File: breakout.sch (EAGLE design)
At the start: 21 parts

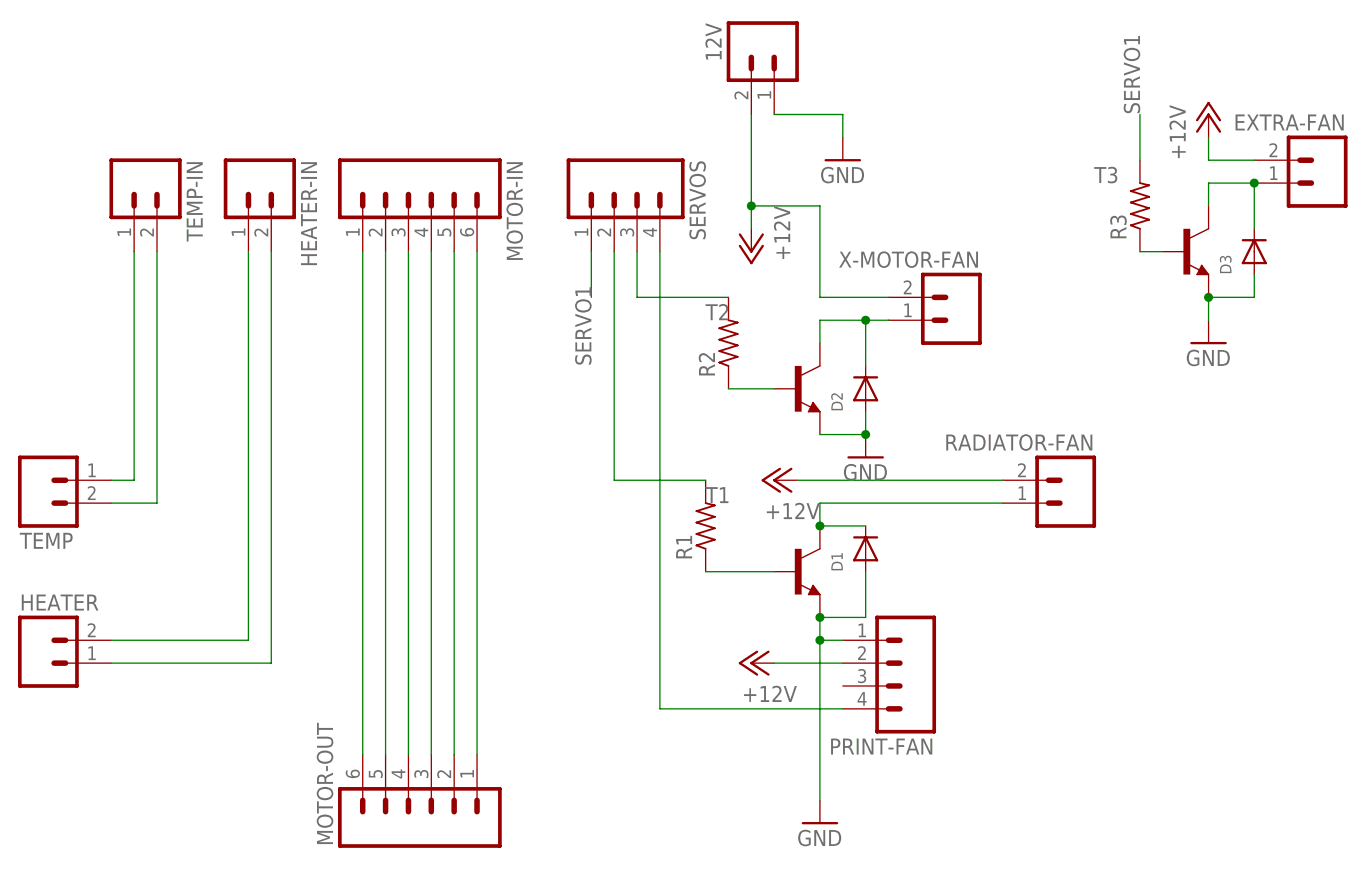
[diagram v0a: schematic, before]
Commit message: Adjusted to 2mm spacing for motor connector, and moved some connectors a bit.
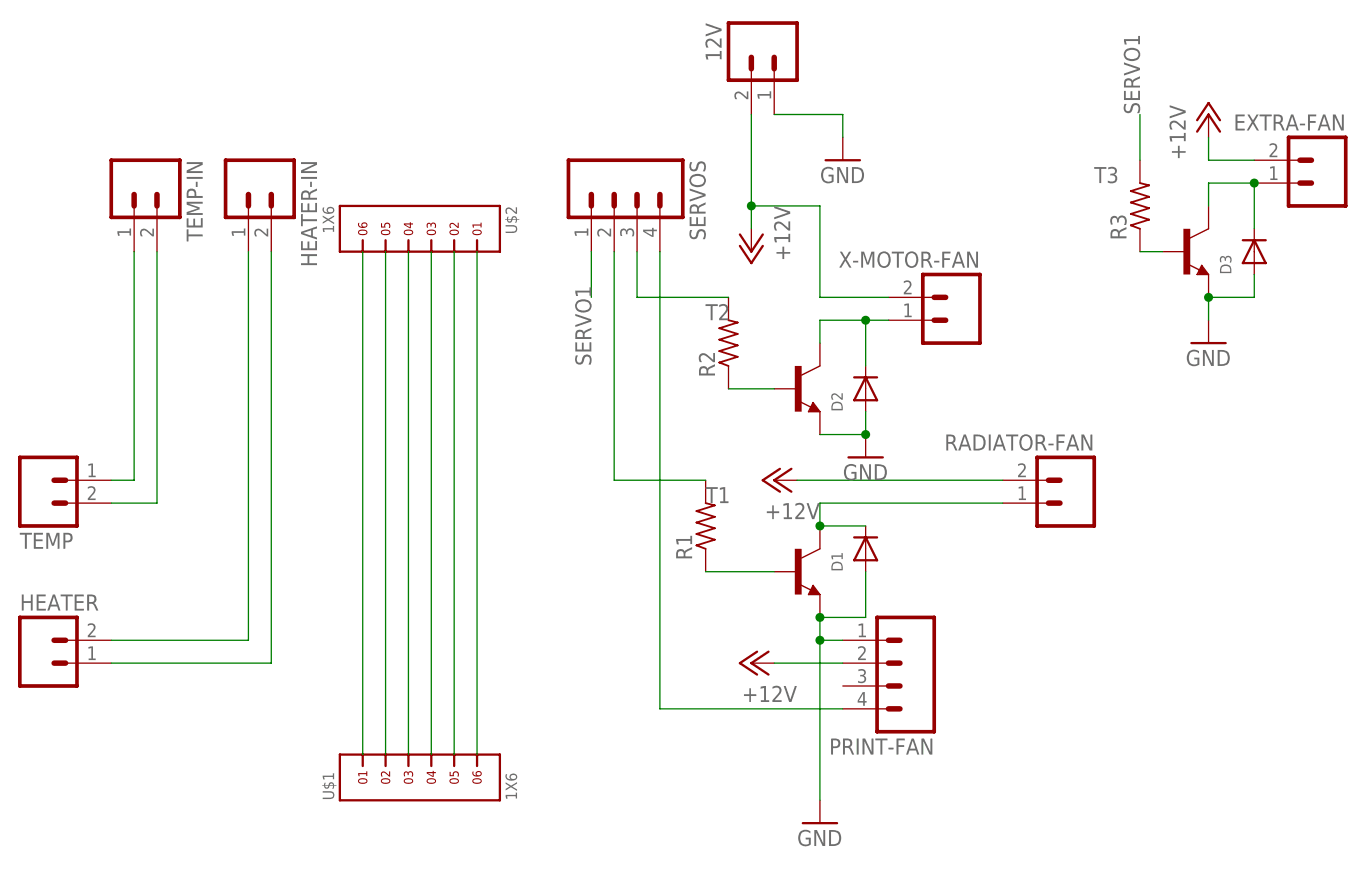
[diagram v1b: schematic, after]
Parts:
- removed MOTOR-IN, MOTOR-OUT: (no value), con-amp-quick:M06
- added U$1, U$2: 1X6, headers(2mm):1X6
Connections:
- net N$1: now also U$1.1, U$2.6; no longer MOTOR-IN.1, MOTOR-OUT.6
- net N$2: now also U$1.2, U$2.5; no longer MOTOR-IN.2, MOTOR-OUT.5
- net N$3: now also U$1.3, U$2.4; no longer MOTOR-IN.3, MOTOR-OUT.4
- net N$4: now also U$1.4, U$2.3; no longer MOTOR-IN.4, MOTOR-OUT.3
- net N$5: now also U$1.5, U$2.2; no longer MOTOR-IN.5, MOTOR-OUT.2
- net N$6: now also U$1.6, U$2.1; no longer MOTOR-IN.6, MOTOR-OUT.1
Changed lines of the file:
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@@
 <?xml version="1.0" encoding="utf-8"?>
 <!DOCTYPE eagle SYSTEM "eagle.dtd">
-<eagle version="7.5.0">
+<eagle version="8.7.0">
 <drawing>
 <settings>
 <setting alwaysvectorfont="no"/>
+<setting keepoldvectorfont="yes"/>
 <setting verticaltext="up"/>
 </settings>
@@
 </classes>
 <parts>
-<part name="MOTOR-OUT" library="con-amp-quick" deviceset="M06" device=""/>
-<part name="MOTOR-IN" library="con-amp-quick" deviceset="M06" device=""/>
 <part name="TEMP" library="con-amp-quick" deviceset="M02" device=""/>
 <part name="HEATER" library="con-amp-quick" deviceset="M02" device=""/>
@@
 <part name="12V" library="con-amp-quick" deviceset="M02" device=""/>
 <part name="GND4" library="supply1" deviceset="GND" device=""/>
+<part name="U$1" library="headers(2mm)" deviceset="1X6" device=""/>
+<part name="U$2" library="headers(2mm)" deviceset="1X6" device=""/>
 </parts>
 <sheets>
@@
 </plain>
 <instances>
-<instance part="MOTOR-OUT" gate="G$1" x="48.26" y="12.7" rot="R90"/>
-<instance part="MOTOR-IN" gate="G$1" x="45.72" y="78.74" rot="R270"/>
 <instance part="TEMP" gate="G$1" x="5.08" y="48.26" rot="MR180"/>
 <instance part="HEATER" gate="G$1" x="5.08" y="27.94"/>
@@
 <instance part="12V" gate="G$1" x="86.36" y="96.52" rot="MR270"/>
 <instance part="GND4" gate="1" x="93.98" y="83.82"/>
+<instance part="U$1" gate="G$1" x="48.26" y="15.24" rot="R90"/>
+<instance part="U$2" gate="G$1" x="45.72" y="76.2" rot="R270"/>
 </instances>
 <busses>
 </busses>
 <nets>
-<net name="N$1" class="0">
-<segment>
-<pinref part="MOTOR-OUT" gate="G$1" pin="6"/>
-<pinref part="MOTOR-IN" gate="G$1" pin="1"/>
-<wire x1="40.64" y1="73.66" x2="40.64" y2="17.78" width="0.1524" layer="91"/>
-</segment>
-</net>
 <net name="N$2" class="0">
 <segment>
-<pinref part="MOTOR-OUT" gate="G$1" pin="5"/>
-<pinref part="MOTOR-IN" gate="G$1" pin="2"/>
 <wire x1="43.18" y1="73.66" x2="43.18" y2="17.78" width="0.1524" layer="91"/>
+<pinref part="U$1" gate="G$1" pin="2"/>
+<pinref part="U$2" gate="G$1" pin="5"/>
 </segment>
 </net>
 <net name="N$3" class="0">
 <segment>
-<pinref part="MOTOR-OUT" gate="G$1" pin="4"/>
-<pinref part="MOTOR-IN" gate="G$1" pin="3"/>
 <wire x1="45.72" y1="73.66" x2="45.72" y2="17.78" width="0.1524" layer="91"/>
+<pinref part="U$1" gate="G$1" pin="3"/>
+<pinref part="U$2" gate="G$1" pin="4"/>
 </segment>
 </net>
 <net name="N$4" class="0">
 <segment>
-<pinref part="MOTOR-OUT" gate="G$1" pin="3"/>
-<pinref part="MOTOR-IN" gate="G$1" pin="4"/>
 <wire x1="48.26" y1="73.66" x2="48.26" y2="17.78" width="0.1524" layer="91"/>
+<pinref part="U$1" gate="G$1" pin="4"/>
+<pinref part="U$2" gate="G$1" pin="3"/>
 </segment>
 </net>
 <net name="N$5" class="0">
 <segment>
-<pinref part="MOTOR-OUT" gate="G$1" pin="2"/>
-<pinref part="MOTOR-IN" gate="G$1" pin="5"/>
 <wire x1="50.8" y1="73.66" x2="50.8" y2="17.78" width="0.1524" layer="91"/>
+<pinref part="U$1" gate="G$1" pin="5"/>
+<pinref part="U$2" gate="G$1" pin="2"/>
 </segment>
 </net>
 <net name="N$6" class="0">
 <segment>
-<pinref part="MOTOR-OUT" gate="G$1" pin="1"/>
-<pinref part="MOTOR-IN" gate="G$1" pin="6"/>
 <wire x1="53.34" y1="73.66" x2="53.34" y2="17.78" width="0.1524" layer="91"/>
+<pinref part="U$1" gate="G$1" pin="6"/>
+<pinref part="U$2" gate="G$1" pin="1"/>
 </segment>
 </net>
@@
 </segment>
 </net>
+<net name="N$1" class="0">
+<segment>
+<pinref part="U$1" gate="G$1" pin="1"/>
+<pinref part="U$2" gate="G$1" pin="6"/>
+<wire x1="40.64" y1="17.78" x2="40.64" y2="73.66" width="0.1524" layer="91"/>
+</segment>
+</net>

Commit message: Adjusting labels and positioning.
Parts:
- renumbered EXTRA-FAN to FAN
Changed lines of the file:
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@@
 <part name="R2" library="adafruit" deviceset="R-US_" device="R0603"/>
 <part name="GND2" library="supply1" deviceset="GND" device=""/>
-<part name="EXTRA-FAN" library="con-amp-quick" deviceset="M02" device=""/>
+<part name="FAN" library="con-amp-quick" deviceset="M02" device=""/>
 <part name="T3" library="transistor" deviceset="*-NPN-" device="SOT23-BEC" technology="BC808"/>
 <part name="D3" library="adafruit" deviceset="DIODE" device="SMA"/>
@@
 <instance part="R2" gate="G$1" x="81.28" y="63.5" rot="R90"/>
 <instance part="GND2" gate="1" x="96.52" y="50.8"/>
-<instance part="EXTRA-FAN" gate="G$1" x="147.32" y="81.28" rot="MR0"/>
+<instance part="FAN" gate="G$1" x="147.32" y="81.28" rot="MR0"/>
 <instance part="T3" gate="G$1" x="132.08" y="73.66"/>
 <instance part="D3" gate="G$1" x="139.7" y="73.66" rot="R90"/>
@@
 </segment>
 <segment>
-<pinref part="EXTRA-FAN" gate="G$1" pin="2"/>
+<pinref part="FAN" gate="G$1" pin="2"/>
 <pinref part="P+2" gate="1" pin="+12V"/>
 <wire x1="139.7" y1="83.82" x2="134.62" y2="83.82" width="0.1524" layer="91"/>
@@
 <segment>
 <pinref part="D3" gate="G$1" pin="C"/>
-<pinref part="EXTRA-FAN" gate="G$1" pin="1"/>
+<pinref part="FAN" gate="G$1" pin="1"/>
 <wire x1="139.7" y1="76.2" x2="139.7" y2="81.28" width="0.1524" layer="91"/>
 <pinref part="T3" gate="G$1" pin="C"/>
